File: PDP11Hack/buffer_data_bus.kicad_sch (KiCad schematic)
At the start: 6 parts, among them U10 74LS573, U11 74LS573, U12 74LS573, U13 74LS245, U14 74LS245, U9 74HCT04

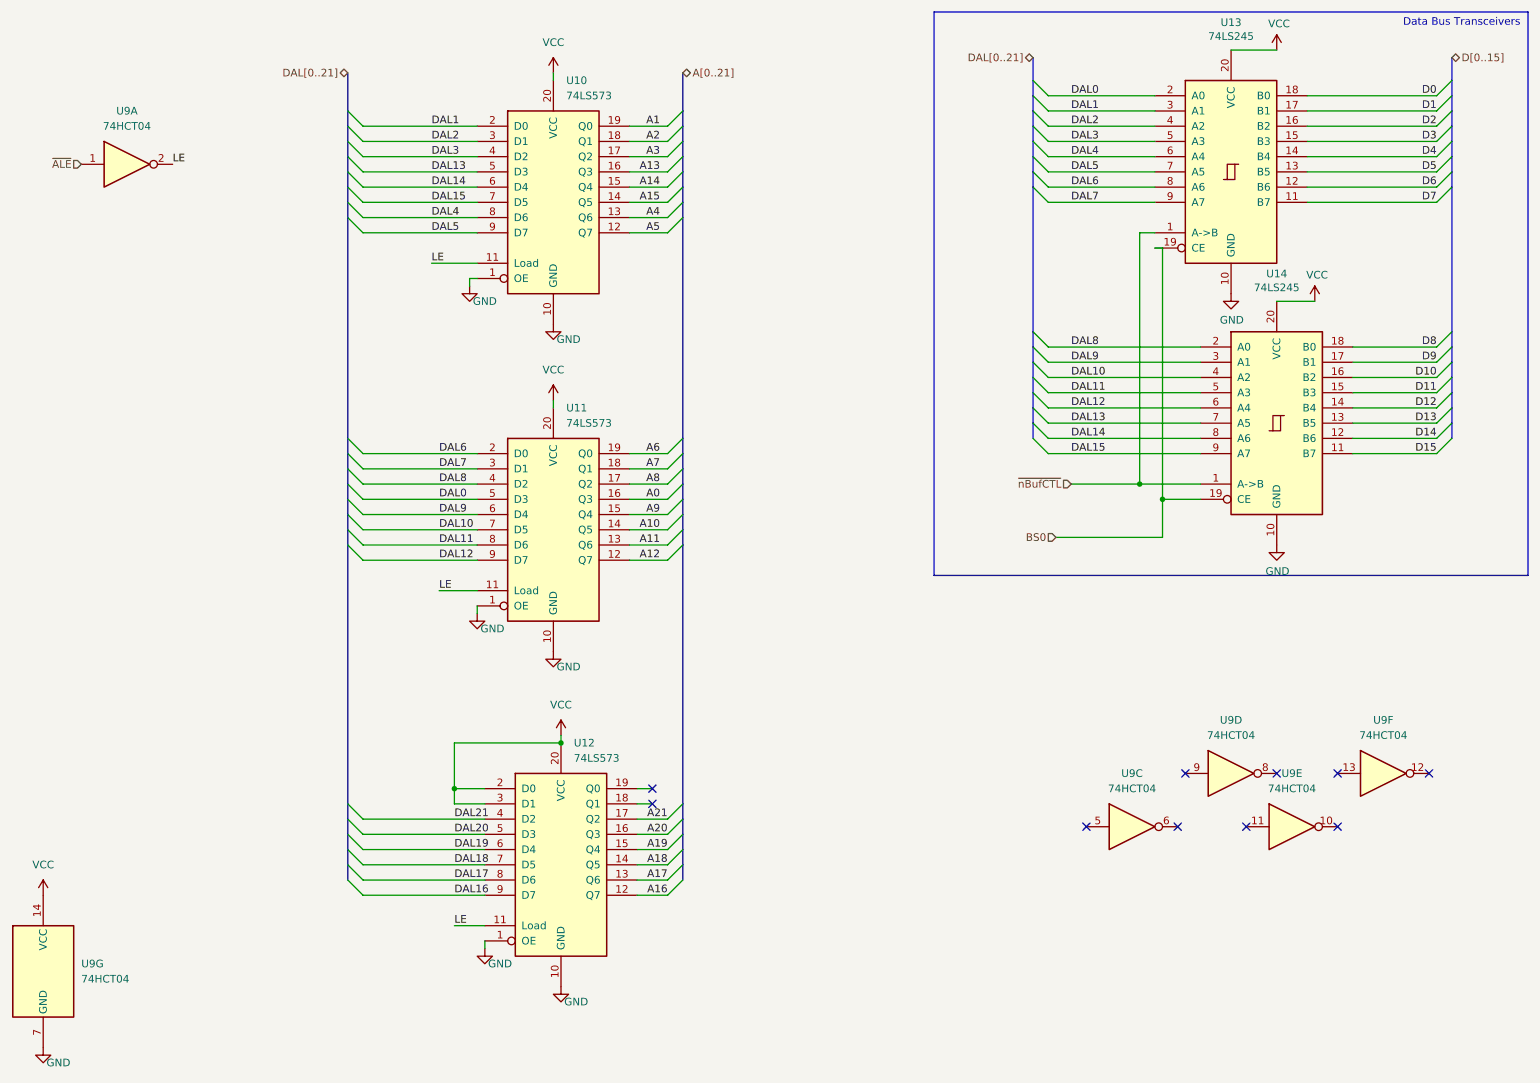
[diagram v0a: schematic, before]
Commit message: Corrections thanks to Peter Schranz on VCFED
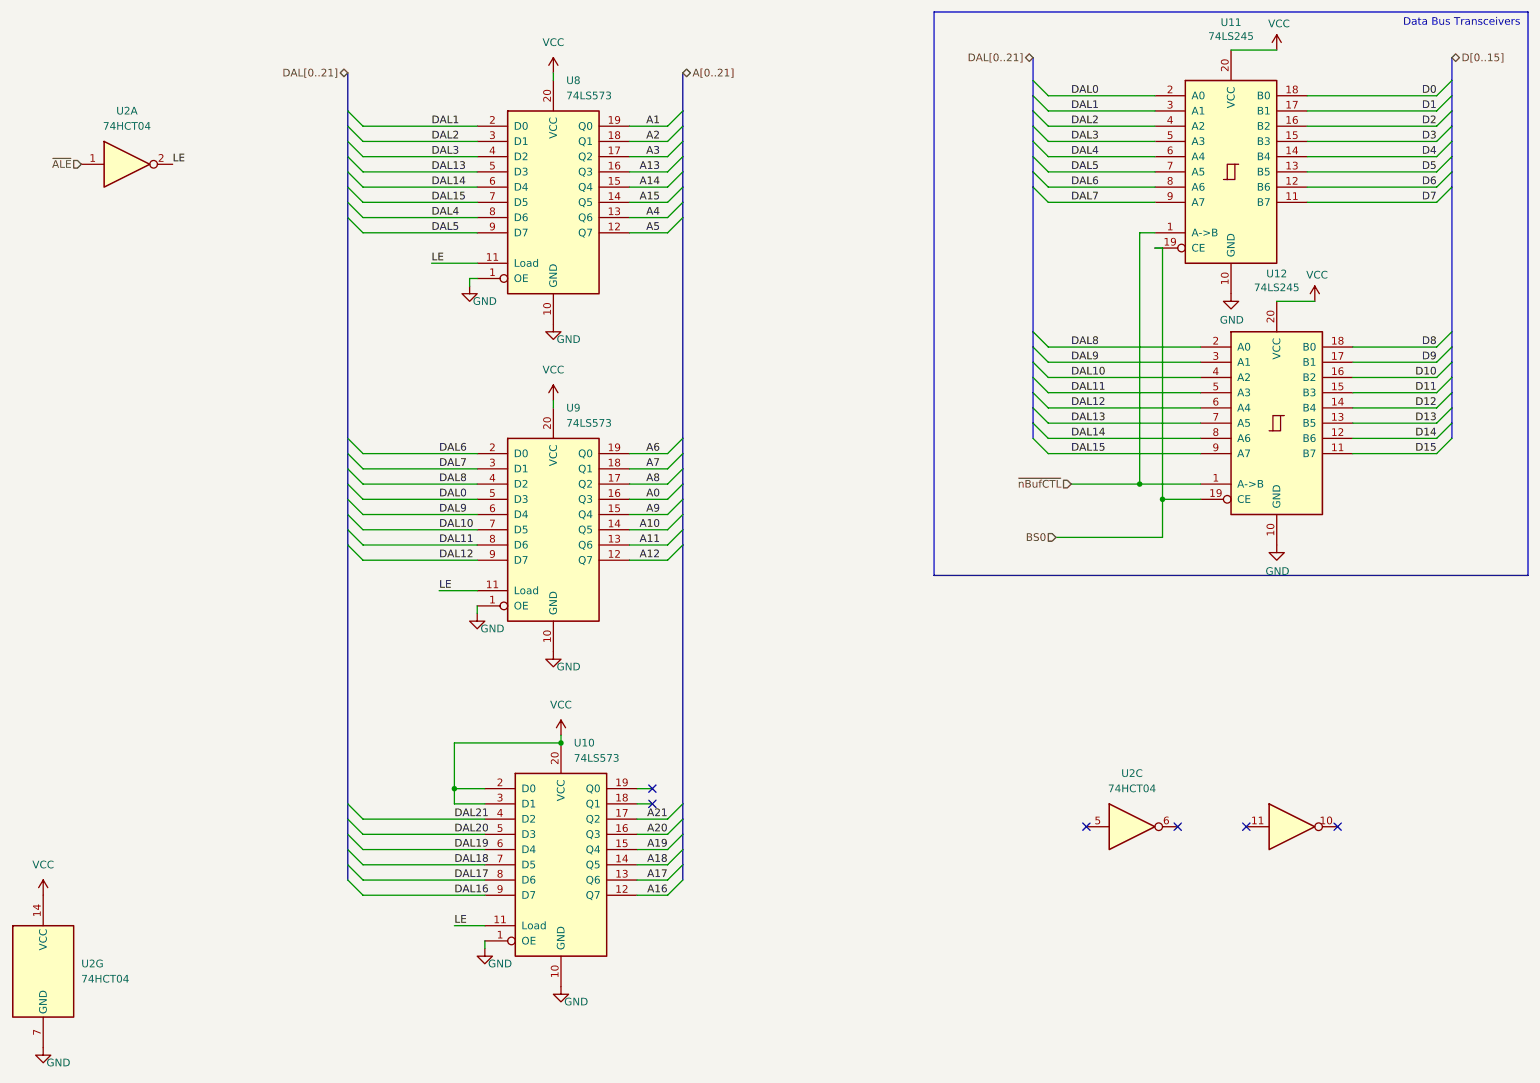
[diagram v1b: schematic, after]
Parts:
- removed unit 6 of U9
- removed unit 4 of U9
- renumbered U12 to U10, U13 to U11, U14 to U12, U9 to U2, U10 to U8, U11 to U9
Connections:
- no-connect marks 10 -> 6

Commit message: Last update, PCB creation ready
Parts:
- removed unit 3 of U2
- U2: footprint (none) -> Package_DIP:DIP-14_W7.62mm
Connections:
- no-connect marks 6 -> 4
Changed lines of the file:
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@@
 	)
 	(no_connect
-		(at 200.66 156.21)
-	)
-	(no_connect
-		(at 215.9 156.21)
-	)
-	(no_connect
 		(at 227.33 156.21)
 	)
@@
 			)
 		)
-		(property "Footprint" ""
+		(property "Footprint" "Package_DIP:DIP-14_W7.62mm"
 			(at 26.67 180.34 0)
 			(effects
@@
 			)
 		)
-		(property "Footprint" ""
+		(property "Footprint" "Package_DIP:DIP-14_W7.62mm"
 			(at 234.95 156.21 0)
 			(effects
@@
 	)
 	(symbol
-		(lib_id "74xx:74HCT04")
-		(at 208.28 156.21 0)
-		(unit 3)
-		(exclude_from_sim no)
-		(in_bom yes)
-		(on_board yes)
-		(dnp no)
-		(fields_autoplaced yes)
-		(property "Reference" "U2"
-			(at 208.28 147.32 0)
-			(effects
-				(font
-					(size 1.27 1.27)
-				)
-			)
-		)
-		(property "Value" "74HCT04"
-			(at 208.28 149.86 0)
-			(effects
-				(font
-					(size 1.27 1.27)
-				)
-			)
-		)
-		(property "Footprint" ""
-			(at 208.28 156.21 0)
-			(effects
-				(font
-					(size 1.27 1.27)
-				)
-				(hide yes)
-			)
-		)
-		(property "Datasheet" "https://assets.nexperia.com/documents/data-sheet/74HC_HCT04.pdf"
-			(at 208.28 156.21 0)
-			(effects
-				(font
-					(size 1.27 1.27)
-				)
-				(hide yes)
-			)
-		)
-		(property "Description" "Hex Inverter"
-			(at 208.28 156.21 0)
-			(effects
-				(font
-					(size 1.27 1.27)
-				)
-				(hide yes)
-			)
-		)
-		(pin "1"
-		)
-		(pin "13"
-		)
-		(pin "12"
-		)
-		(pin "7"
-		)
-		(pin "14"
-		)
-		(pin "9"
-		)
-		(pin "10"
-		)
-		(pin "8"
-		)
-		(pin "3"
-		)
-		(pin "4"
-		)
-		(pin "5"
-		)
-		(pin "2"
-		)
-		(pin "6"
-		)
-		(pin "11"
-		)
-		(instances
-			(project ""
-				(path "/264d9b66-53d1-4564-94e8-42c7c0bb6a66/8cc463d2-0973-425f-a093-4bae22165332"
-					(reference "U2")
-					(unit 3)
-				)
-			)
-		)
-	)
-	(symbol
 		(lib_id "power:GND")
 		(at 232.41 109.22 0)
@@
 			)
 		)
-		(property "Footprint" ""
+		(property "Footprint" "Package_DIP:DIP-14_W7.62mm"
 			(at 40.64 45.72 0)
 			(effects
